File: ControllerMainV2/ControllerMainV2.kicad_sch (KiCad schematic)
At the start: 13 parts, among them J1 Conn_01x06, J2 Conn_01x10, U1 MCP23009-E_SO, U2 MCP23009-E_SO

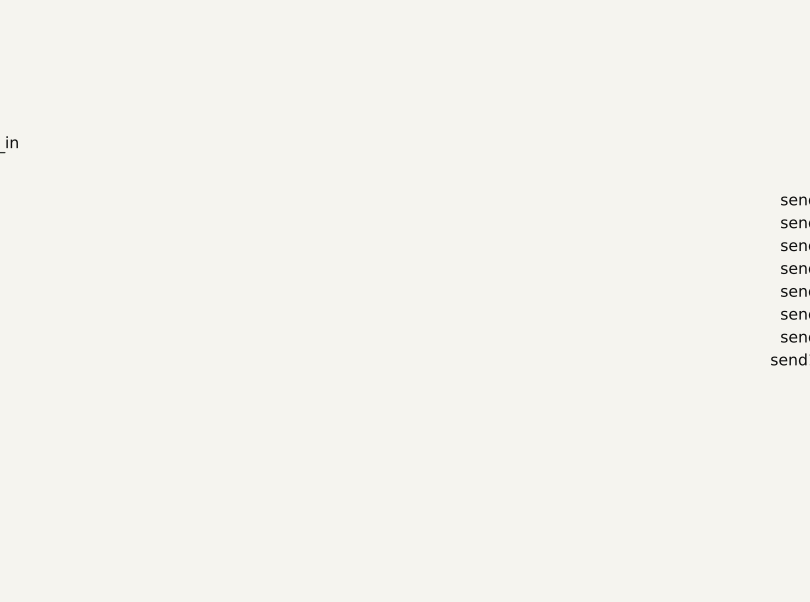
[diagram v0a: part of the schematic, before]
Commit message: Enclosure and faceplate for 8 loops
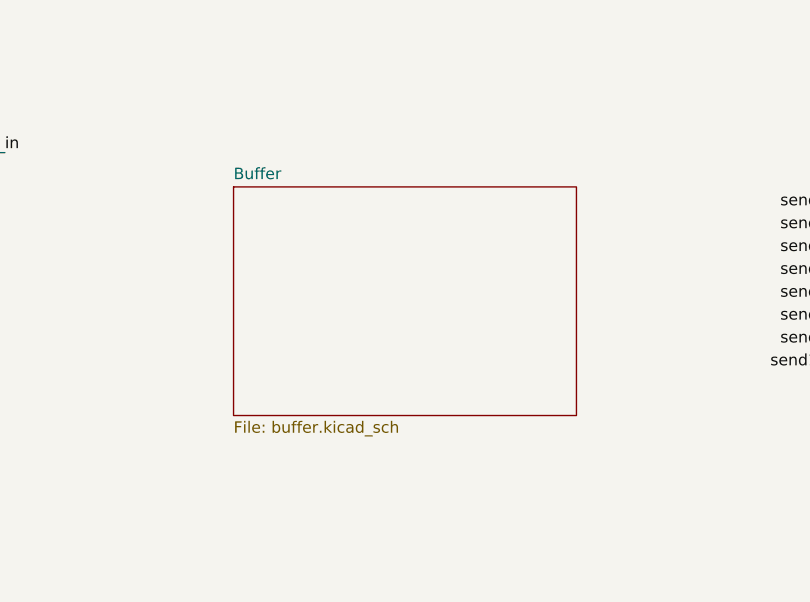
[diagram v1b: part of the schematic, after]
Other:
- added sheet Buffer (buffer.kicad_sch)
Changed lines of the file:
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@@
+    )
+  )
+  (sheet (at 149.86 154.94) (size 38.1 25.4) (fields_autoplaced)
+    (stroke (width 0.1524) (type solid) (color 0 0 0 0))
+    (fill (color 0 0 0 0.0000))
+    (property "Sheet name" "Buffer" (id 0) (at 149.86 154.2284 0)
+      (effects (font (size 1.27 1.27)) (justify left bottom))
+    )
+    (property "Sheet file" "buffer.kicad_sch" (id 1) (at 149.86 180.9246 0)
+      (effects (font (size 1.27 1.27)) (justify left top))
     )
   )
@@
     (path "/2b30f0e6-367c-4784-a8f8-1e47807d1c67" (page "6"))
     (path "/96fedf5b-a5e1-40d9-8616-8018f29ca7bc" (page "7"))
+    (path "/7aa0426e-2e69-40f4-85c6-96114512afe4" (page "8"))
   )
   (symbol_instances
@@
       (reference "#PWR0127") (unit 1) (value "GND") (footprint "")
     )
+    (path "/7aa0426e-2e69-40f4-85c6-96114512afe4/10a9d742-53a3-417c-a9b4-85a327ceb07e"
+      (reference "#PWR?") (unit 1) (value "GND") (footprint "")
+    )
+    (path "/7aa0426e-2e69-40f4-85c6-96114512afe4/654990e8-47e2-44ce-9320-6e3e4872c756"
+      (reference "#PWR?") (unit 1) (value "GND") (footprint "")
+    )
+    (path "/7aa0426e-2e69-40f4-85c6-96114512afe4/664e37ed-fd0c-405c-a942-e1e222aa4ae9"
+      (reference "#PWR?") (unit 1) (value "GND") (footprint "")
+    )
+    (path "/7aa0426e-2e69-40f4-85c6-96114512afe4/a019f83e-84ee-4223-b27d-48b648ece2c5"
+      (reference "#PWR?") (unit 1) (value "GND") (footprint "")
+    )
+    (path "/7aa0426e-2e69-40f4-85c6-96114512afe4/c75c0cfc-9a14-4b8e-aff1-6efa8dea59ff"
+      (reference "#PWR?") (unit 1) (value "GND") (footprint "")
+    )
+    (path "/7aa0426e-2e69-40f4-85c6-96114512afe4/df60a457-51db-4a9c-8e4e-84ca25344478"
+      (reference "#PWR?") (unit 1) (value "GND") (footprint "")
+    )
     (path "/00000000-0000-0000-0000-0000618cd10b/1f5db387-92a0-4bf6-9034-11f2272fc48b"
       (reference "C1") (unit 1) (value "100n") (footprint "Capacitor_SMD:C_1206_3216Metric_Pad1.33x1.80mm_HandSolder")
@@
       (reference "C31") (unit 1) (value "10u") (footprint "Capacitor_SMD:C_1206_3216Metric_Pad1.33x1.80mm_HandSolder")
     )
+    (path "/7aa0426e-2e69-40f4-85c6-96114512afe4/06412d67-d43a-465b-9867-29f09191892e"
+      (reference "C?") (unit 1) (value "1u") (footprint "Capacitor_SMD:C_1206_3216Metric_Pad1.33x1.80mm_HandSolder")
+    )
+    (path "/7aa0426e-2e69-40f4-85c6-96114512afe4/2e89c012-fc31-4703-8147-cf96fa430890"
+      (reference "C?") (unit 1) (value "1u") (footprint "Capacitor_SMD:C_1206_3216Metric_Pad1.33x1.80mm_HandSolder")
+    )
+    (path "/7aa0426e-2e69-40f4-85c6-96114512afe4/72cc273f-6c7e-45bb-a6a7-463bbb127104"
+      (reference "C?") (unit 1) (value "22n") (footprint "Capacitor_SMD:C_1206_3216Metric_Pad1.33x1.80mm_HandSolder")
+    )
+    (path "/7aa0426e-2e69-40f4-85c6-96114512afe4/c9d23920-e138-4da3-b592-3eb55d42ad72"
+      (reference "C?") (unit 1) (value "22n") (footprint "Capacitor_SMD:C_1206_3216Metric_Pad1.33x1.80mm_HandSolder")
+    )
     (path "/3f5cd97e-7933-4ec6-a055-3b3284744af6"
       (reference "C_Spl1") (unit 1) (value "100n") (footprint "Capacitor_SMD:C_1206_3216Metric_Pad1.33x1.80mm_HandSolder")
@@
       (reference "IC27") (unit 1) (value "1462039-4") (footprint "SamacSys_Parts:14620394")
     )
+    (path "/7aa0426e-2e69-40f4-85c6-96114512afe4/96530f96-0296-4aa9-9de6-f92a90442bf0"
+      (reference "IC?") (unit 1) (value "AD5293BRUZ-20-RL7") (footprint "SOP65P640X120-14N")
+    )
     (path "/af90eea0-5fb9-4e56-8f45-5ede5d49b1aa"
       (reference "J1") (unit 1) (value "Conn_01x06") (footprint "Connector_JST:JST_PH_B6B-PH-K_1x06_P2.00mm_Vertical")
@@
     )
     (path "/00000000-0000-0000-0000-0000618cd10b/3ad86930-6ccb-4be9-8a0b-a559e7e86db5"
-      (reference "R22") (unit 1) (value "4.7M") (footprint "Resistor_SMD:R_1206_3216Metric_Pad1.30x1.75mm_HandSolder")
+      (reference "R22") (unit 1) (value "2.2M") (footprint "Resistor_SMD:R_1206_3216Metric_Pad1.30x1.75mm_HandSolder")
     )
     (path "/00000000-0000-0000-0000-0000618cd10b/fab56c50-1bb0-42dd-8b53-8d330e29adcb"
-      (reference "R23") (unit 1) (value "4.7M") (footprint "Resistor_SMD:R_1206_3216Metric_Pad1.30x1.75mm_HandSolder")
+      (reference "R23") (unit 1) (value "2.2M") (footprint "Resistor_SMD:R_1206_3216Metric_Pad1.30x1.75mm_HandSolder")
     )
     (path "/00000000-0000-0000-0000-0000618cd10b/6b275b84-721c-4ec9-8031-292e0e961b42"
-      (reference "R24") (unit 1) (value "4.7M") (footprint "Resistor_SMD:R_1206_3216Metric_Pad1.30x1.75mm_HandSolder")
+      (reference "R24") (unit 1) (value "2.2M") (footprint "Resistor_SMD:R_1206_3216Metric_Pad1.30x1.75mm_HandSolder")
     )
     (path "/00000000-0000-0000-0000-0000618cd10b/027d8cb8-5cfc-49e7-bc4d-9077a1ee9c68"
-      (reference "R25") (unit 1) (value "4.7M") (footprint "Resistor_SMD:R_1206_3216Metric_Pad1.30x1.75mm_HandSolder")
+      (reference "R25") (unit 1) (value "2.2M") (footprint "Resistor_SMD:R_1206_3216Metric_Pad1.30x1.75mm_HandSolder")
     )
     (path "/00000000-0000-0000-0000-0000618cd10b/bb99b453-3bdf-4e5d-834b-1077a28ea944"
-      (reference "R26") (unit 1) (value "4.7M") (footprint "Resistor_SMD:R_1206_3216Metric_Pad1.30x1.75mm_HandSolder")
+      (reference "R26") (unit 1) (value "2.2M") (footprint "Resistor_SMD:R_1206_3216Metric_Pad1.30x1.75mm_HandSolder")
     )
     (path "/00000000-0000-0000-0000-0000618cd10b/e5f11666-525f-49a0-a19c-1739f49bd85a"
-      (reference "R27") (unit 1) (value "4.7M") (footprint "Resistor_SMD:R_1206_3216Metric_Pad1.30x1.75mm_HandSolder")
+      (reference "R27") (unit 1) (value "2.2M") (footprint "Resistor_SMD:R_1206_3216Metric_Pad1.30x1.75mm_HandSolder")
     )
     (path "/00000000-0000-0000-0000-0000618cd10b/4dca8d34-e6e5-4333-9c80-2ec01effe3a2"
-      (reference "R28") (unit 1) (value "4.7M") (footprint "Resistor_SMD:R_1206_3216Metric_Pad1.30x1.75mm_HandSolder")
+      (reference "R28") (unit 1) (value "2.2M") (footprint "Resistor_SMD:R_1206_3216Metric_Pad1.30x1.75mm_HandSolder")
     )
     (path "/00000000-0000-0000-0000-0000618cd10b/8ba4a521-d251-4a08-8749-890fb3226751"
-      (reference "R29") (unit 1) (value "4.7M") (footprint "Resistor_SMD:R_1206_3216Metric_Pad1.30x1.75mm_HandSolder")
+      (reference "R29") (unit 1) (value "2.2M") (footprint "Resistor_SMD:R_1206_3216Metric_Pad1.30x1.75mm_HandSolder")
     )
     (path "/00000000-0000-0000-0000-0000618cd10b/678511a7-4bcb-4241-aaa4-9764b40214c8"
@@
       (reference "R70") (unit 1) (value "1k") (footprint "Resistor_SMD:R_1206_3216Metric_Pad1.30x1.75mm_HandSolder")
     )
+    (path "/7aa0426e-2e69-40f4-85c6-96114512afe4/5ee1dd7c-b6dc-48bf-a0c5-4e8f8710a773"
+      (reference "R?") (unit 1) (value "100") (footprint "Resistor_SMD:R_1206_3216Metric_Pad1.30x1.75mm_HandSolder")
+    )
+    (path "/7aa0426e-2e69-40f4-85c6-96114512afe4/61d564a0-a408-4610-b1c1-f6719ca84707"
+      (reference "R?") (unit 1) (value "100k") (footprint "Resistor_SMD:R_1206_3216Metric_Pad1.30x1.75mm_HandSolder")
+    )
+    (path "/7aa0426e-2e69-40f4-85c6-96114512afe4/8078ebe6-f6ed-46a2-ba20-51128aef59e8"
+      (reference "R?") (unit 1) (value "2.2M") (footprint "Resistor_SMD:R_1206_3216Metric_Pad1.30x1.75mm_HandSolder")
+    )
+    (path "/7aa0426e-2e69-40f4-85c6-96114512afe4/ae669a75-3f17-4348-b6b0-931bea5ea0e0"
+      (reference "R?") (unit 1) (value "100k") (footprint "Resistor_SMD:R_1206_3216Metric_Pad1.30x1.75mm_HandSolder")
+    )
+    (path "/7aa0426e-2e69-40f4-85c6-96114512afe4/b01002fd-60cd-47e3-963e-df57dd1ead31"
+      (reference "R?") (unit 1) (value "2.2M") (footprint "Resistor_SMD:R_1206_3216Metric_Pad1.30x1.75mm_HandSolder")
+    )
+    (path "/7aa0426e-2e69-40f4-85c6-96114512afe4/bff704e3-1933-46be-b183-a391f6ea5227"
+      (reference "R?") (unit 1) (value "2.2M") (footprint "Resistor_SMD:R_1206_3216Metric_Pad1.30x1.75mm_HandSolder")
+    )
+    (path "/7aa0426e-2e69-40f4-85c6-96114512afe4/c98c2928-dff5-4423-bb74-3634c6b2b22a"
+      (reference "R?") (unit 1) (value "100") (footprint "Resistor_SMD:R_1206_3216Metric_Pad1.30x1.75mm_HandSolder")
+    )
+    (path "/7aa0426e-2e69-40f4-85c6-96114512afe4/d8362335-e0a1-48e4-a25d-0f2f0713d4f4"
+      (reference "R?") (unit 1) (value "2.2M") (footprint "Resistor_SMD:R_1206_3216Metric_Pad1.30x1.75mm_HandSolder")
+    )
     (path "/00000000-0000-0000-0000-000061b51d86/af2cf04d-a89f-487a-86d4-bf7b2176e12a"
       (reference "T1") (unit 1) (value "Lehle_MZ_P") (footprint "Lehle_Transformer:Lehle_MZ_P")
@@
       (reference "U18") (unit 5) (value "TL074") (footprint "SamacSys_Parts:SOIC127P600X175-14N")
     )
+    (path "/7aa0426e-2e69-40f4-85c6-96114512afe4/b43f8fc7-2991-4cfc-a413-4febffef1ea5"
+      (reference "U?") (unit 1) (value "TL074") (footprint "")
+    )
+    (path "/7aa0426e-2e69-40f4-85c6-96114512afe4/c69c3920-b3c3-4ea9-a162-f5416daae23f"
+      (reference "U?") (unit 1) (value "TL072") (footprint "")
+    )
+    (path "/7aa0426e-2e69-40f4-85c6-96114512afe4/12a20b03-4fde-4cd5-9517-6d1a3067085b"
+      (reference "U?") (unit 2) (value "TL072") (footprint "")
+    )
+    (path "/7aa0426e-2e69-40f4-85c6-96114512afe4/7c5a6a9c-4b61-4e03-9cb6-04f22c289cd1"
+      (reference "U?") (unit 2) (value "TL074") (footprint "")
+    )
+    (path "/7aa0426e-2e69-40f4-85c6-96114512afe4/8de71e1d-7562-46ea-b942-d00b6419f68a"
+      (reference "U?") (unit 3) (value "TL074") (footprint "")
+    )
+    (path "/7aa0426e-2e69-40f4-85c6-96114512afe4/a6899599-66b8-4979-8b3c-2959f25d84ea"
+      (reference "U?") (unit 3) (value "TL072") (footprint "")
+    )
+    (path "/7aa0426e-2e69-40f4-85c6-96114512afe4/fb9e1a67-ce87-4315-b4c3-6ac0143cde3a"
+      (reference "U?") (unit 4) (value "TL074") (footprint "")
+    )
+    (path "/7aa0426e-2e69-40f4-85c6-96114512afe4/9954dd71-cea6-43eb-8492-1515660aada6"
+      (reference "U?") (unit 5) (value "TL074") (footprint "")
+    )
   )

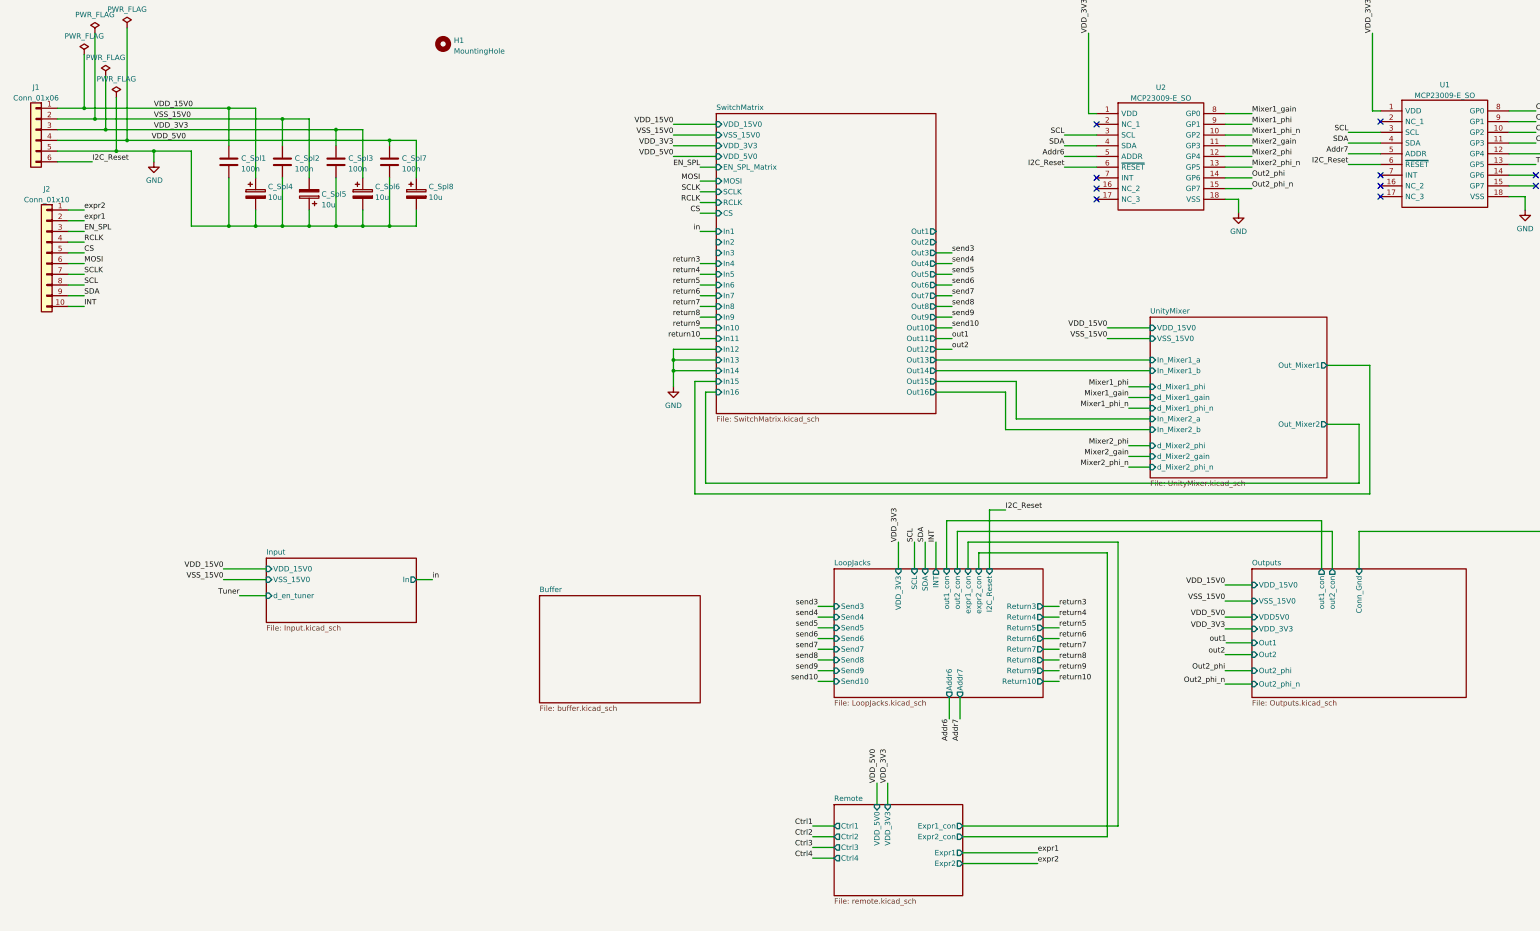
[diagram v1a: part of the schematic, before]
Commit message: Added amp schematic
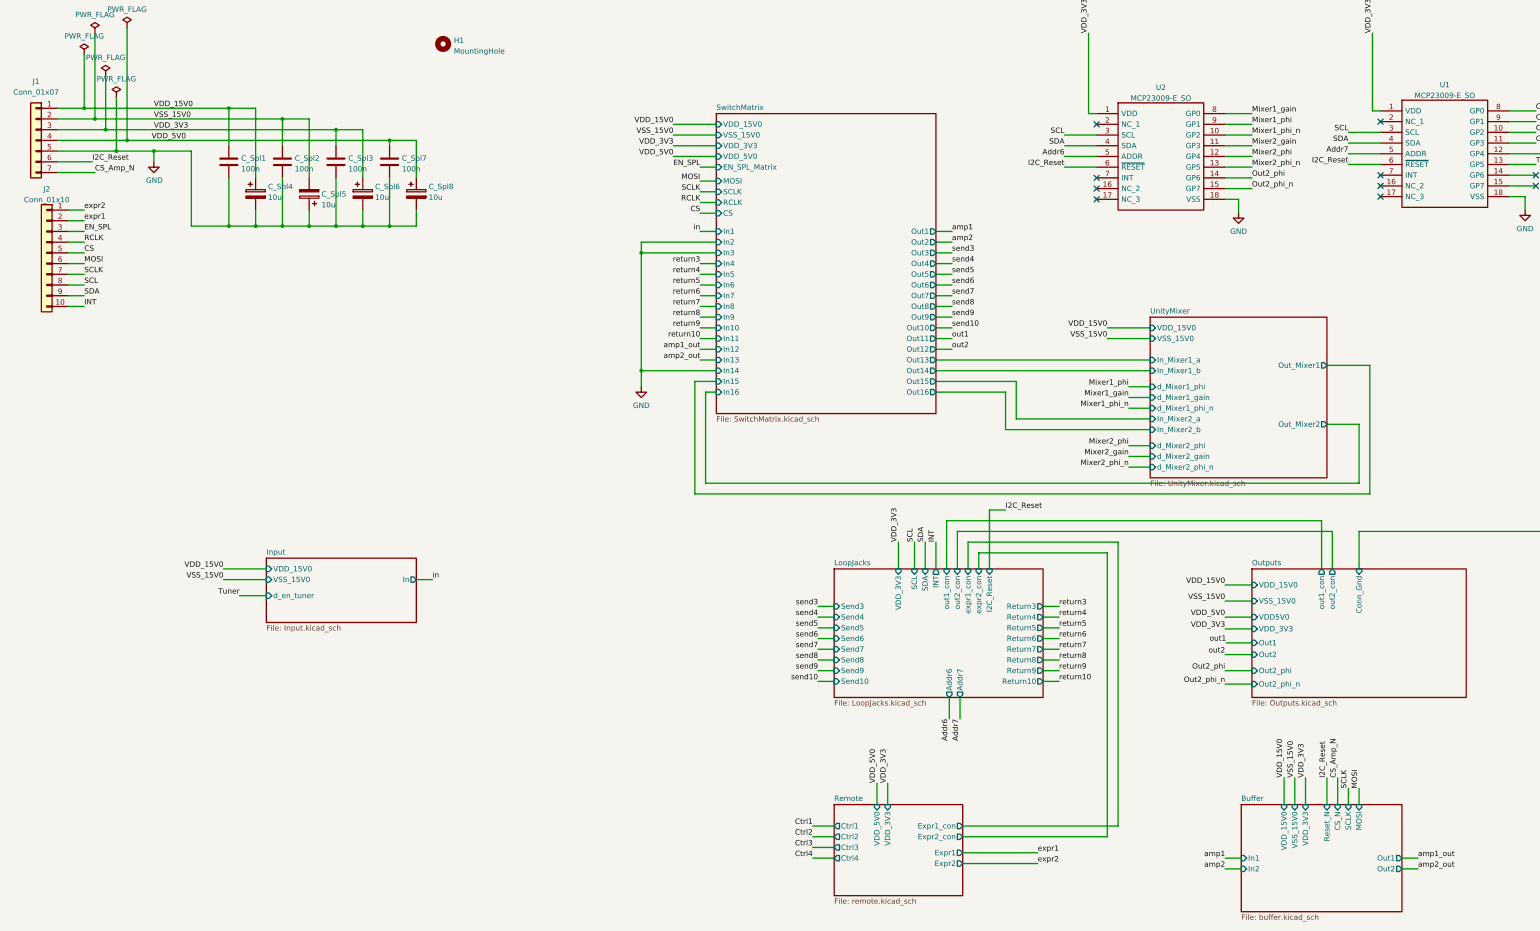
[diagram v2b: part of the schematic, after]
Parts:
- removed J1: Conn_01x06, Connector_JST:JST_PH_B6B-PH-K_1x06_P2.00mm_Vertical, symbol Connector_Generic:Conn_01x06
- added J1: Conn_01x07, symbol Connector_Generic:Conn_01x07
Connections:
- net GND: now also J1.5 (Pin_5)
- net I2C_Reset: now also J1.6 (Pin_6)
- net VDD_15V0: now also J1.1 (Pin_1)
- net VDD_3V3: now also J1.3 (Pin_3)
- net VDD_5V0: now also J1.4 (Pin_4)
- net VSS_15V0: now also J1.2 (Pin_2)
- new net CS_Amp_N: J1.7 (Pin_7)
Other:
- sheet Buffer ports: added CS_N, In1, In2, MOSI, Out1, Out2, Reset_N, SCLK, VDD_15V0, VDD_3V3, VSS_15V0; removed none
